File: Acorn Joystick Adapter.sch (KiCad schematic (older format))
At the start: 16 parts

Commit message: Single port, second as placeholder
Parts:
- added J3: Atari #2, Connectors_DSub:DSUB-9_Male_Horizontal_Pitch2.77x2.54mm_EdgePinOffset9.40mm, symbol Atari_Joystick
- J1: renamed from J?; footprint (none) -> Connectors_DSub:DSUB-15_Male_Horizontal_Pitch2.77x2.54mm_EdgePinOffset9.40mm; symbol DB15_Male -> BBC_Analog
- J2: renamed from J?; value Atari -> Atari #1; footprint (none) -> Connectors_DSub:DSUB-9_Male_Horizontal_Pitch2.77x2.54mm_EdgePinOffset9.40mm; symbol DB9_Male -> Atari_Joystick
- R1, R10, R11, R2, R3, R4, R5, R6, R7, R8, R9: renamed from R?; footprint (none) -> Resistors_THT:R_Axial_DIN0207_L6.3mm_D2.5mm_P10.16mm_Horizontal
- gave numbers to parts that had none: 3
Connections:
- net B_CH0 is gone; now on net A_LEFT: J1.15 (P15)
- net B_CH1 is gone; now on net A_UP: J1.7
- net A_GND: no longer J1.14 (P14)
- no-connect marks 12 -> 22

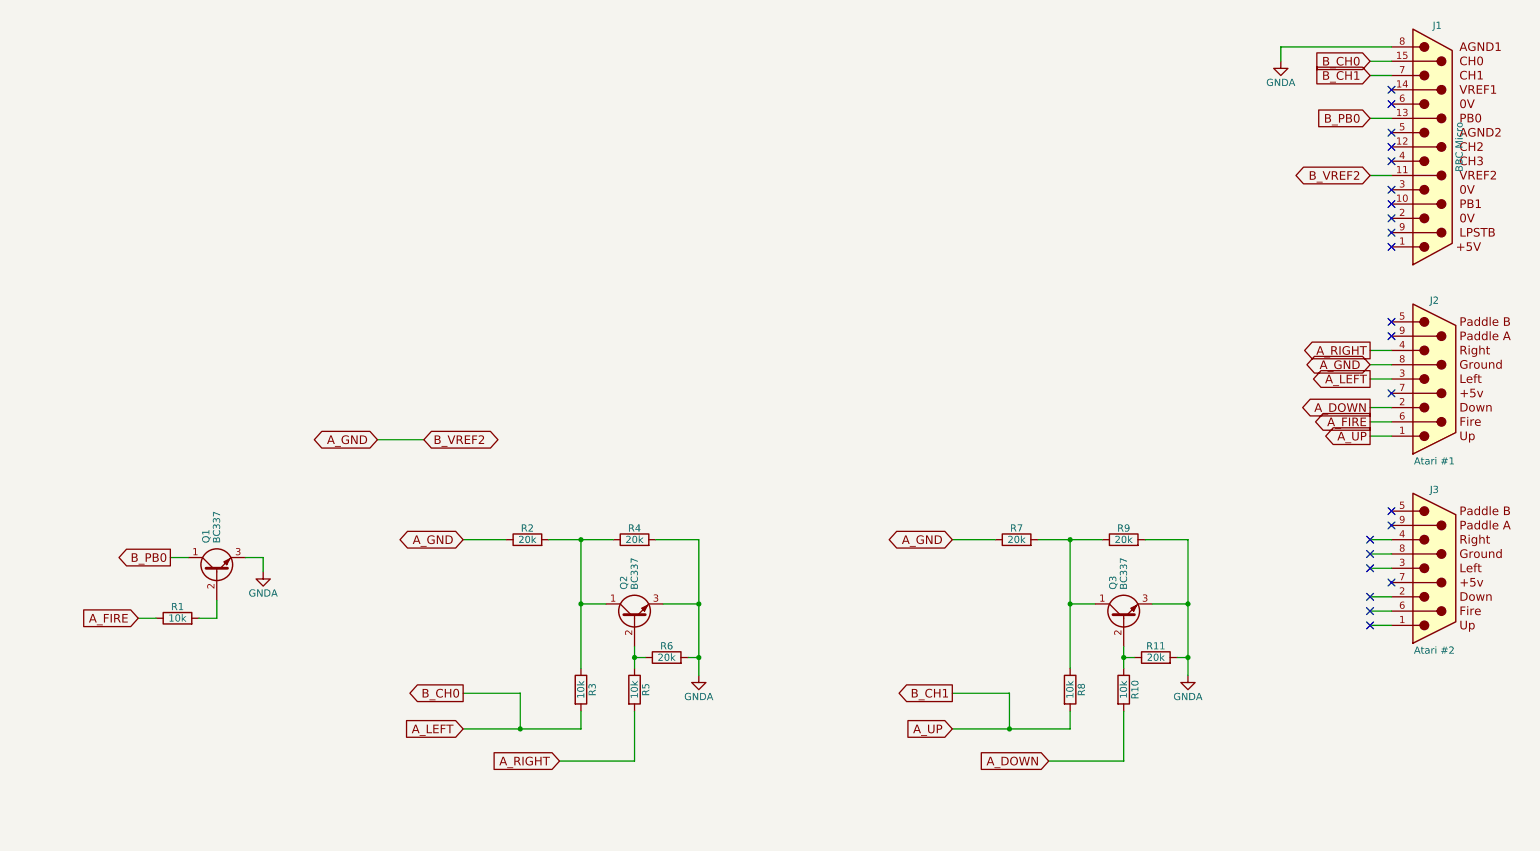
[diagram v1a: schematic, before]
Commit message: Added second joystick port to schematic
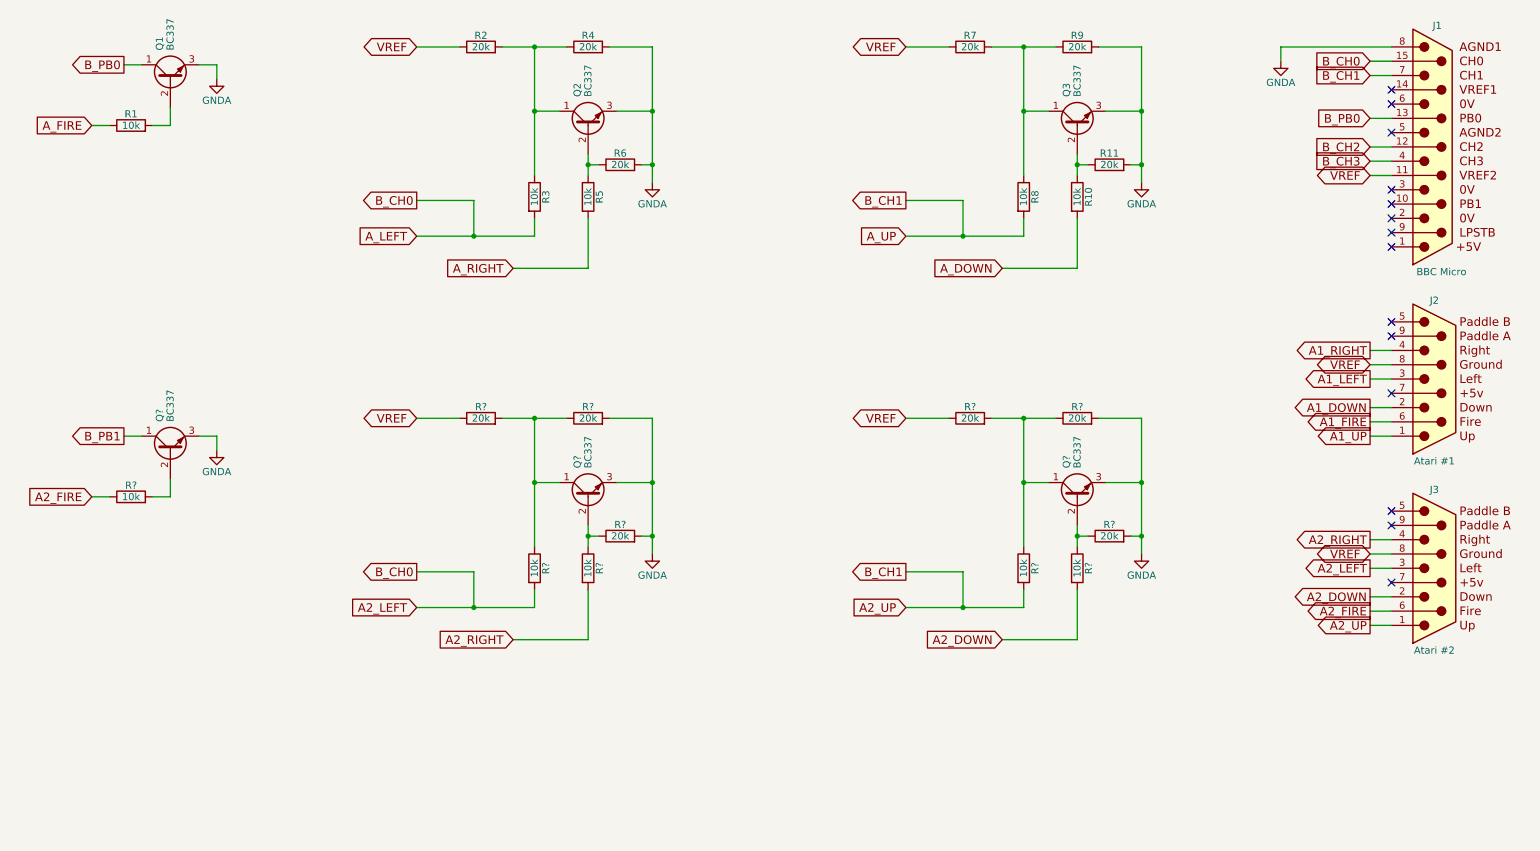
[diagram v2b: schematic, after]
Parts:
- added Q? (x3): BC337, TO_SOT_Packages_THT:TO-92_Molded_Narrow, symbol BC337
- added R? (x5): 10k, Resistors_THT:R_Axial_DIN0207_L6.3mm_D2.5mm_P10.16mm_Horizontal, symbol R
- added R? (x6): 20k, Resistors_THT:R_Axial_DIN0207_L6.3mm_D2.5mm_P10.16mm_Horizontal, symbol R
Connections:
- net A_GND is gone; now on net VREF: J1.11 (P111), J2.8, R2.1, R7.1
- net A_DOWN: no longer J2.2
- net A_FIRE: no longer J2.6
- net A_RIGHT: no longer J2.4
- net GNDA: now also Q?.3 (E), Q?.3 (E), Q?.3 (E), R?.2, R?.2, R?.2, R?.2
- net B_CH2: now reaches J1.12 (P12)
- net B_CH3: now reaches J1.4
- net A2_UP: now reaches J3.1
- net A2_UP: now also J1.7, R8.2, R?.2
- net A2_DOWN: now reaches J3.2
- net A2_DOWN: now also R?.2
- net A2_LEFT: now reaches J3.3
- net A2_LEFT: now also J1.15 (P15), R3.2, R?.2
- net A2_RIGHT: now reaches J3.4
- net A2_RIGHT: now also R?.2
- net A2_FIRE: now reaches J3.6
- net A2_FIRE: now also R?.1
- net VREF: now reaches J3.8
- net VREF: now also R?.1, R?.1
- removed net A_LEFT: J1.15 (P15), J2.3, R3.2
- removed net A_UP: J1.7, J2.1, R8.2
- new net: Q?.2 (B), R?.2
- new net: Q?.1 (C), R?.1, R?.1, R?.2 (x2)
- new net: Q?.2 (B), R?.1, R?.1 (x2)
- new net A1_DOWN: J2.2
- new net A1_FIRE: J2.6
- new net A1_LEFT: J2.3
- new net A1_RIGHT: J2.4
- new net A1_UP: J2.1
- new net B_PB1: Q?.1 (C)
- no-connect marks 22 -> 14
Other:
- moved on the sheet: Q1, Q2, Q3, R1, R10, R11, R2, R3, R4, R5, R6, R7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

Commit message: Changed transistor footprint and pcb layout
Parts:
- J1: value BBC Micro -> Acorn Computer; footprint Connectors_DSub:DSUB-15_Male_Horizontal_Pitch2.77x2.54mm_EdgePinOffset9.40mm -> Connectors_DSub:DSUB-15_Male_Vertical_Pitch2.77x2.84mm
- J2, J3: footprint Connectors_DSub:DSUB-9_Male_Horizontal_Pitch2.77x2.54mm_EdgePinOffset9.40mm -> Connectors_DSub:DSUB-9_Male_Vertical_Pitch2.77x2.84mm
- Q1, Q2, Q3: footprint TO_SOT_Packages_THT:TO-92_Molded_Narrow -> TO_SOT_Packages_THT:TO-92_Inline_Narrow_Oval
- Q4, Q5, Q6: renamed from Q?; footprint TO_SOT_Packages_THT:TO-92_Molded_Narrow -> TO_SOT_Packages_THT:TO-92_Inline_Narrow_Oval
- gave numbers to parts that had none: 11
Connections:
- net A_DOWN is gone; now on net A1_DOWN: R10.2
- net A_FIRE is gone; now on net A1_FIRE: R1.1
- net A_RIGHT is gone; now on net A1_RIGHT: R5.2
- net B_CH2 is gone; now on net A2_LEFT: J1.12 (P12)
- net B_CH3 is gone; now on net A2_UP: J1.4
- net A1_LEFT: now also J1.15 (P15), R3.2
- net A1_UP: now also J1.7, R8.2
- net A2_LEFT: no longer J1.15 (P15), R3.2
- net A2_UP: no longer J1.7, R8.2
- net B_PB1: now also J1.10 (P10)
- no-connect marks 14 -> 13
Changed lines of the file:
@@
 P 10500 1550
 F 0 "J1" H 10520 2400 50  0000 C CNN
-F 1 "BBC Micro" H 10550 675 50  0000 C CNN
-F 2 "Connectors_DSub:DSUB-15_Male_Horizontal_Pitch2.77x2.54mm_EdgePinOffset9.40mm" H 10500 1550 50  0001 C CNN
+F 1 "Acorn Computer" H 10550 675 50  0000 C CNN
+F 2 "Connectors_DSub:DSUB-15_Male_Vertical_Pitch2.77x2.84mm" H 10500 1550 50  0001 C CNN
 F 3 "" H 10500 1550 50  0001 C CNN
 	1    10500 1550
@@
 F 0 "J2" H 10500 3725 50  0000 C CNN
 F 1 "Atari #1" H 10500 2600 50  0000 C CNN
-F 2 "Connectors_DSub:DSUB-9_Male_Horizontal_Pitch2.77x2.54mm_EdgePinOffset9.40mm" H 10500 3175 50  0001 C CNN
+F 2 "Connectors_DSub:DSUB-9_Male_Vertical_Pitch2.77x2.84mm" H 10500 3175 50  0001 C CNN
 F 3 "" H 10500 3175 50  0001 C CNN
 	1    10500 3175
@@
 NoConn ~ 10200 1250
 NoConn ~ 10200 2150
-NoConn ~ 10200 1950
 Wire Wire Line
 	10200 3075 10050 3075
@@
 F 0 "Q1" H 1850 1150 50  0000 L CNN
 F 1 "BC337" H 1850 1075 50  0000 L CNN
-F 2 "TO_SOT_Packages_THT:TO-92_Molded_Narrow" H 1850 1000 50  0001 L CIN
+F 2 "TO_SOT_Packages_THT:TO-92_Inline_Narrow_Oval" H 1850 1000 50  0001 L CIN
 F 3 "" H 1650 1075 50  0001 L CNN
 	1    1650 1075
@@
 $EndComp
 Text GLabel 1100 1400 0    60   Input ~ 0
-A_FIRE
+A1_FIRE
 Wire Wire Line
 	1650 1275 1650 1400
@@
 F 0 "Q2" H 4775 1475 50  0000 L CNN
 F 1 "BC337" H 4775 1400 50  0000 L CNN
-F 2 "TO_SOT_Packages_THT:TO-92_Molded_Narrow" H 4775 1325 50  0001 L CIN
+F 2 "TO_SOT_Packages_THT:TO-92_Inline_Narrow_Oval" H 4775 1325 50  0001 L CIN
 F 3 "" H 4575 1400 50  0001 L CNN
 	1    4575 1400
@@
 Connection ~ 4575 1675
 Text GLabel 4050 2400 0    60   Input ~ 0
-A_RIGHT
+A1_RIGHT
 Wire Wire Line
 	4575 2050 4575 2400
@@
 	4575 2400 4050 2400
 Text GLabel 3375 2175 0    60   Input ~ 0
-A_LEFT
+A1_LEFT
 $Comp
 L R R4
@@
 F 0 "Q3" H 8200 1475 50  0000 L CNN
 F 1 "BC337" H 8200 1400 50  0000 L CNN
-F 2 "TO_SOT_Packages_THT:TO-92_Molded_Narrow" H 8200 1325 50  0001 L CIN
+F 2 "TO_SOT_Packages_THT:TO-92_Inline_Narrow_Oval" H 8200 1325 50  0001 L CIN
 F 3 "" H 8000 1400 50  0001 L CNN
 	1    8000 1400
@@
 	8000 2400 7475 2400
 Text GLabel 6800 2175 0    60   Input ~ 0
-A_UP
+A1_UP
 $Comp
 L R R9
@@
 	6800 850  7100 850
 Text GLabel 7475 2400 0    60   Input ~ 0
-A_DOWN
+A1_DOWN
 Text GLabel 10050 1750 0    60   BiDi ~ 0
 VREF
@@
 F 0 "J3" H 10500 5050 50  0000 C CNN
 F 1 "Atari #2" H 10500 3925 50  0000 C CNN
-F 2 "Connectors_DSub:DSUB-9_Male_Horizontal_Pitch2.77x2.54mm_EdgePinOffset9.40mm" H 10500 4500 50  0001 C CNN
+F 2 "Connectors_DSub:DSUB-9_Male_Vertical_Pitch2.77x2.84mm" H 10500 4500 50  0001 C CNN
 F 3 "" H 10500 4500 50  0001 C CNN
 	1    10500 4500
@@
 VREF
 $Comp
-L BC337 Q?
+L BC337 Q4
 U 1 1 5BAFF15A
 P 1650 3675
-F 0 "Q?" H 1850 3750 50  0000 L CNN
+F 0 "Q4" H 1850 3750 50  0000 L CNN
 F 1 "BC337" H 1850 3675 50  0000 L CNN
-F 2 "TO_SOT_Packages_THT:TO-92_Molded_Narrow" H 1850 3600 50  0001 L CIN
+F 2 "TO_SOT_Packages_THT:TO-92_Inline_Narrow_Oval" H 1850 3600 50  0001 L CIN
 F 3 "" H 1650 3675 50  0001 L CNN
 	1    1650 3675
@@
 	1450 3575 1325 3575
 $Comp
-L R R?
+L R R12
 U 1 1 5BAFF162
 P 1375 4000
-F 0 "R?" V 1455 4000 50  0000 C CNN
+F 0 "R12" V 1455 4000 50  0000 C CNN
 F 1 "10k" V 1375 4000 50  0000 C CNN
 F 2 "Resistors_THT:R_Axial_DIN0207_L6.3mm_D2.5mm_P10.16mm_Horizontal" V 1305 4000 50  0001 C CNN
@@
 	1100 4000 1225 4000
 $Comp
-L GNDA #PWR?
+L GNDA #PWR05
 U 1 1 5BAFF16C
 P 1975 3675
-F 0 "#PWR?" H 1975 3425 50  0001 C CNN
+F 0 "#PWR05" H 1975 3425 50  0001 C CNN
 F 1 "GNDA" H 1975 3525 50  0000 C CNN
 F 2 "" H 1975 3675 50  0001 C CNN
@@
 	1975 3575 1850 3575
 $Comp
-L BC337 Q?
+L BC337 Q5
 U 1 1 5BAFF174
 P 4575 4000
-F 0 "Q?" H 4775 4075 50  0000 L CNN
+F 0 "Q5" H 4775 4075 50  0000 L CNN
 F 1 "BC337" H 4775 4000 50  0000 L CNN
-F 2 "TO_SOT_Packages_THT:TO-92_Molded_Narrow" H 4775 3925 50  0001 L CIN
+F 2 "TO_SOT_Packages_THT:TO-92_Inline_Narrow_Oval" H 4775 3925 50  0001 L CIN
 F 3 "" H 4575 4000 50  0001 L CNN
 	1    4575 4000
@@
 $EndComp
 $Comp
-L GNDA #PWR?
+L GNDA #PWR06
 U 1 1 5BAFF17A
 P 5025 4400
-F 0 "#PWR?" H 5025 4150 50  0001 C CNN
+F 0 "#PWR06" H 5025 4150 50  0001 C CNN
 F 1 "GNDA" H 5025 4250 50  0000 C CNN
 F 2 "" H 5025 4400 50  0001 C CNN
@@
 	4775 3900 5025 3900
 $Comp
-L R R?
+L R R17
 U 1 1 5BAFF182
 P 4800 4275
-F 0 "R?" V 4880 4275 50  0000 C CNN
+F 0 "R17" V 4880 4275 50  0000 C CNN
 F 1 "20k" V 4800 4275 50  0000 C CNN
 F 2 "Resistors_THT:R_Axial_DIN0207_L6.3mm_D2.5mm_P10.16mm_Horizontal" V 4730 4275 50  0001 C CNN
@@
 	4575 4275 4650 4275
 $Comp
-L R R?
+L R R16
 U 1 1 5BAFF18C
 P 4575 4500
-F 0 "R?" V 4655 4500 50  0000 C CNN
+F 0 "R16" V 4655 4500 50  0000 C CNN
 F 1 "10k" V 4575 4500 50  0000 C CNN
 F 2 "Resistors_THT:R_Axial_DIN0207_L6.3mm_D2.5mm_P10.16mm_Horizontal" V 4505 4500 50  0001 C CNN
@@
 A2_LEFT
 $Comp
-L R R?
+L R R15
 U 1 1 5BAFF197
 P 4575 3450
-F 0 "R?" V 4655 3450 50  0000 C CNN
+F 0 "R15" V 4655 3450 50  0000 C CNN
 F 1 "20k" V 4575 3450 50  0000 C CNN
 F 2 "Resistors_THT:R_Axial_DIN0207_L6.3mm_D2.5mm_P10.16mm_Horizontal" V 4505 3450 50  0001 C CNN
@@
 $EndComp
 $Comp
-L R R?
+L R R14
 U 1 1 5BAFF19D
 P 4200 4500
-F 0 "R?" V 4280 4500 50  0000 C CNN
+F 0 "R14" V 4280 4500 50  0000 C CNN
 F 1 "10k" V 4200 4500 50  0000 C CNN
 F 2 "Resistors_THT:R_Axial_DIN0207_L6.3mm_D2.5mm_P10.16mm_Horizontal" V 4130 4500 50  0001 C CNN
@@
 Connection ~ 5025 3900
 $Comp
-L R R?
+L R R13
 U 1 1 5BAFF1AA
 P 3825 3450
-F 0 "R?" V 3905 3450 50  0000 C CNN
+F 0 "R13" V 3905 3450 50  0000 C CNN
 F 1 "20k" V 3825 3450 50  0000 C CNN
 F 2 "Resistors_THT:R_Axial_DIN0207_L6.3mm_D2.5mm_P10.16mm_Horizontal" V 3755 3450 50  0001 C CNN
@@
 	3375 3450 3675 3450
 $Comp
-L BC337 Q?
+L BC337 Q6
 U 1 1 5BAFF1B2
 P 8000 4000
-F 0 "Q?" H 8200 4075 50  0000 L CNN
+F 0 "Q6" H 8200 4075 50  0000 L CNN
 F 1 "BC337" H 8200 4000 50  0000 L CNN
-F 2 "TO_SOT_Packages_THT:TO-92_Molded_Narrow" H 8200 3925 50  0001 L CIN
+F 2 "TO_SOT_Packages_THT:TO-92_Inline_Narrow_Oval" H 8200 3925 50  0001 L CIN
 F 3 "" H 8000 4000 50  0001 L CNN
 	1    8000 4000
@@
 $EndComp
 $Comp
-L GNDA #PWR?
+L GNDA #PWR07
 U 1 1 5BAFF1B8
 P 8450 4400
-F 0 "#PWR?" H 8450 4150 50  0001 C CNN
+F 0 "#PWR07" H 8450 4150 50  0001 C CNN
 F 1 "GNDA" H 8450 4250 50  0000 C CNN
 F 2 "" H 8450 4400 50  0001 C CNN
@@
 	8200 3900 8450 3900
 $Comp
-L R R?
+L R R22
 U 1 1 5BAFF1C0
 P 8225 4275
-F 0 "R?" V 8305 4275 50  0000 C CNN
+F 0 "R22" V 8305 4275 50  0000 C CNN
 F 1 "20k" V 8225 4275 50  0000 C CNN
 F 2 "Resistors_THT:R_Axial_DIN0207_L6.3mm_D2.5mm_P10.16mm_Horizontal" V 8155 4275 50  0001 C CNN
@@
 	8000 4275 8075 4275
 $Comp
-L R R?
+L R R21
 U 1 1 5BAFF1CA
 P 8000 4500
-F 0 "R?" V 8080 4500 50  0000 C CNN
+F 0 "R21" V 8080 4500 50  0000 C CNN
 F 1 "10k" V 8000 4500 50  0000 C CNN
 F 2 "Resistors_THT:R_Axial_DIN0207_L6.3mm_D2.5mm_P10.16mm_Horizontal" V 7930 4500 50  0001 C CNN
@@
 A2_UP
 $Comp
-L R R?
+L R R20
 U 1 1 5BAFF1D4
 P 8000 3450
-F 0 "R?" V 8080 3450 50  0000 C CNN
+F 0 "R20" V 8080 3450 50  0000 C CNN
 F 1 "20k" V 8000 3450 50  0000 C CNN
 F 2 "Resistors_THT:R_Axial_DIN0207_L6.3mm_D2.5mm_P10.16mm_Horizontal" V 7930 3450 50  0001 C CNN
@@
 $EndComp
 $Comp
-L R R?
+L R R19
 U 1 1 5BAFF1DA
 P 7625 4500
-F 0 "R?" V 7705 4500 50  0000 C CNN
+F 0 "R19" V 7705 4500 50  0000 C CNN
 F 1 "10k" V 7625 4500 50  0000 C CNN
 F 2 "Resistors_THT:R_Axial_DIN0207_L6.3mm_D2.5mm_P10.16mm_Horizontal" V 7555 4500 50  0001 C CNN
@@
 Connection ~ 8450 3900
 $Comp
-L R R?
+L R R18
 U 1 1 5BAFF1E8
 P 7250 3450
-F 0 "R?" V 7330 3450 50  0000 C CNN
+F 0 "R18" V 7330 3450 50  0000 C CNN
 F 1 "20k" V 7250 3450 50  0000 C CNN
 F 2 "Resistors_THT:R_Axial_DIN0207_L6.3mm_D2.5mm_P10.16mm_Horizontal" V 7180 3450 50  0001 C CNN
@@
 A2_DOWN
 Text GLabel 6800 4525 0    60   Output ~ 0
-B_CH1
+B_CH3
 Wire Wire Line
 	6800 4525 7200 4525
@@
 Connection ~ 3775 4775
 Text GLabel 3375 4525 0    60   Output ~ 0
-B_CH0
+B_CH2
 Text GLabel 3375 3450 0    60   BiDi ~ 0
 VREF
@@
 Wire Wire Line
 	10050 1650 10200 1650
+Text GLabel 10050 1950 0    60   Input ~ 0
+B_PB1
+Wire Wire Line
+	10050 1950 10200 1950
 $EndSCHEMATC

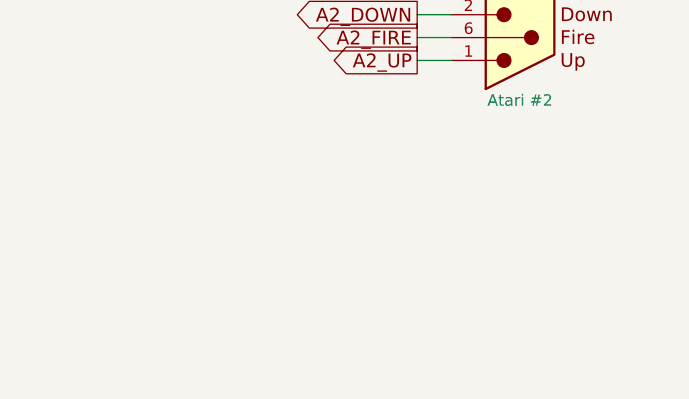
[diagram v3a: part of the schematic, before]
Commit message: Added analog breakout header
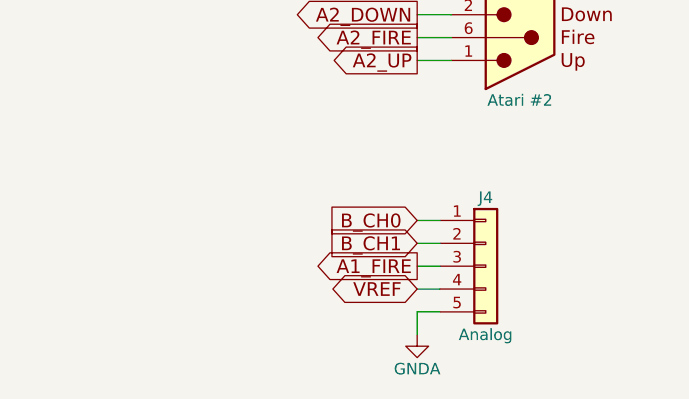
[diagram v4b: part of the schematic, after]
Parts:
- added J4: Analog, Pin_Headers:Pin_Header_Straight_1x05_Pitch2.54mm, symbol Conn_01x05
- J1: footprint Connectors_DSub:DSUB-15_Male_Vertical_Pitch2.77x2.84mm -> RND_DSUB:DSUB-15_Male_Vertical_Pitch2.77x2.84mm
- J2, J3: footprint Connectors_DSub:DSUB-9_Male_Vertical_Pitch2.77x2.84mm -> RND_DSUB:DSUB-9_Male_Vertical_Pitch2.77x2.84mm
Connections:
- net A1_FIRE: now also J4.3 (Pin_3)
- net A1_LEFT: now also J4.1 (Pin_1)
- net A1_UP: now also J4.2 (Pin_2)
- net GNDA: now also J4.5 (Pin_5)
- net VREF: now also J4.4 (Pin_4)
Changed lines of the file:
@@
 F 0 "J1" H 10520 2400 50  0000 C CNN
 F 1 "Acorn Computer" H 10550 675 50  0000 C CNN
-F 2 "Connectors_DSub:DSUB-15_Male_Vertical_Pitch2.77x2.84mm" H 10500 1550 50  0001 C CNN
+F 2 "RND_DSUB:DSUB-15_Male_Vertical_Pitch2.77x2.84mm" H 10500 1550 50  0001 C CNN
 F 3 "" H 10500 1550 50  0001 C CNN
 	1    10500 1550
@@
 F 0 "J2" H 10500 3725 50  0000 C CNN
 F 1 "Atari #1" H 10500 2600 50  0000 C CNN
-F 2 "Connectors_DSub:DSUB-9_Male_Vertical_Pitch2.77x2.84mm" H 10500 3175 50  0001 C CNN
+F 2 "RND_DSUB:DSUB-9_Male_Vertical_Pitch2.77x2.84mm" H 10500 3175 50  0001 C CNN
 F 3 "" H 10500 3175 50  0001 C CNN
 	1    10500 3175
@@
 F 0 "J3" H 10500 5050 50  0000 C CNN
 F 1 "Atari #2" H 10500 3925 50  0000 C CNN
-F 2 "Connectors_DSub:DSUB-9_Male_Vertical_Pitch2.77x2.84mm" H 10500 4500 50  0001 C CNN
+F 2 "RND_DSUB:DSUB-9_Male_Vertical_Pitch2.77x2.84mm" H 10500 4500 50  0001 C CNN
 F 3 "" H 10500 4500 50  0001 C CNN
 	1    10500 4500
@@
 Wire Wire Line
 	10050 1950 10200 1950
+$Comp
+L Conn_01x05 J4
+U 1 1 5BB0FAAF
+P 10350 5800
+F 0 "J4" H 10350 6100 50  0000 C CNN
+F 1 "Analog" H 10350 5500 50  0000 C CNN
+F 2 "Pin_Headers:Pin_Header_Straight_1x05_Pitch2.54mm" H 10350 5800 50  0001 C CNN
+F 3 "" H 10350 5800 50  0001 C CNN
+	1    10350 5800
+	1    0    0    -1
+$EndComp
+Text GLabel 10050 5600 0    60   Input ~ 0
+B_CH0
+Text GLabel 10050 5700 0    60   Input ~ 0
+B_CH1
+Wire Wire Line
+	10050 5600 10150 5600
+Wire Wire Line
+	10050 5700 10150 5700
+Text GLabel 10050 5800 0    60   Output ~ 0
+A1_FIRE
+Wire Wire Line
+	10050 5800 10150 5800
+Text GLabel 10050 5900 0    60   BiDi ~ 0
+VREF
+$Comp
+L GNDA #PWR08
+U 1 1 5BB12497
+P 10050 6100
+F 0 "#PWR08" H 10050 5850 50  0001 C CNN
+F 1 "GNDA" H 10050 5950 50  0000 C CNN
+F 2 "" H 10050 6100 50  0001 C CNN
+F 3 "" H 10050 6100 50  0001 C CNN
+	1    10050 6100
+	1    0    0    -1
+$EndComp
+Wire Wire Line
+	10050 5900 10150 5900
+Wire Wire Line
+	10150 6000 10050 6000
+Wire Wire Line
+	10050 6000 10050 6100
 $EndSCHEMATC

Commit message: Changed transistor footprint (easier to solder)
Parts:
- Q1, Q2, Q3, Q4, Q5, Q6: footprint TO_SOT_Packages_THT:TO-92_Inline_Narrow_Oval -> TO_SOT_Packages_THT:TO-92_Inline_Wide
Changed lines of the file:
@@
 F 0 "Q1" H 1850 1150 50  0000 L CNN
 F 1 "BC337" H 1850 1075 50  0000 L CNN
-F 2 "TO_SOT_Packages_THT:TO-92_Inline_Narrow_Oval" H 1850 1000 50  0001 L CIN
+F 2 "TO_SOT_Packages_THT:TO-92_Inline_Wide" H 1850 1000 50  0001 L CIN
 F 3 "" H 1650 1075 50  0001 L CNN
 	1    1650 1075
@@
 F 0 "Q2" H 4775 1475 50  0000 L CNN
 F 1 "BC337" H 4775 1400 50  0000 L CNN
-F 2 "TO_SOT_Packages_THT:TO-92_Inline_Narrow_Oval" H 4775 1325 50  0001 L CIN
+F 2 "TO_SOT_Packages_THT:TO-92_Inline_Wide" H 4775 1325 50  0001 L CIN
 F 3 "" H 4575 1400 50  0001 L CNN
 	1    4575 1400
@@
 F 0 "Q3" H 8200 1475 50  0000 L CNN
 F 1 "BC337" H 8200 1400 50  0000 L CNN
-F 2 "TO_SOT_Packages_THT:TO-92_Inline_Narrow_Oval" H 8200 1325 50  0001 L CIN
+F 2 "TO_SOT_Packages_THT:TO-92_Inline_Wide" H 8200 1325 50  0001 L CIN
 F 3 "" H 8000 1400 50  0001 L CNN
 	1    8000 1400
@@
 F 0 "Q4" H 1850 3750 50  0000 L CNN
 F 1 "BC337" H 1850 3675 50  0000 L CNN
-F 2 "TO_SOT_Packages_THT:TO-92_Inline_Narrow_Oval" H 1850 3600 50  0001 L CIN
+F 2 "TO_SOT_Packages_THT:TO-92_Inline_Wide" H 1850 3600 50  0001 L CIN
 F 3 "" H 1650 3675 50  0001 L CNN
 	1    1650 3675
@@
 F 0 "Q5" H 4775 4075 50  0000 L CNN
 F 1 "BC337" H 4775 4000 50  0000 L CNN
-F 2 "TO_SOT_Packages_THT:TO-92_Inline_Narrow_Oval" H 4775 3925 50  0001 L CIN
+F 2 "TO_SOT_Packages_THT:TO-92_Inline_Wide" H 4775 3925 50  0001 L CIN
 F 3 "" H 4575 4000 50  0001 L CNN
 	1    4575 4000
@@
 F 0 "Q6" H 8200 4075 50  0000 L CNN
 F 1 "BC337" H 8200 4000 50  0000 L CNN
-F 2 "TO_SOT_Packages_THT:TO-92_Inline_Narrow_Oval" H 8200 3925 50  0001 L CIN
+F 2 "TO_SOT_Packages_THT:TO-92_Inline_Wide" H 8200 3925 50  0001 L CIN
 F 3 "" H 8000 4000 50  0001 L CNN
 	1    8000 4000
